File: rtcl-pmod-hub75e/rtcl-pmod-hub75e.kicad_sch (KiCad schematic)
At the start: 22 parts, among them J1 PMOD, J2 HIF3FC-16PA-2.54DSA(71), J3 Conn_01x02, U1 74LVC273, U2 74LVC273, U3 74LVC273, U4 74LVC273, U5 LM809M3-2.93, U6 74LVC2G86

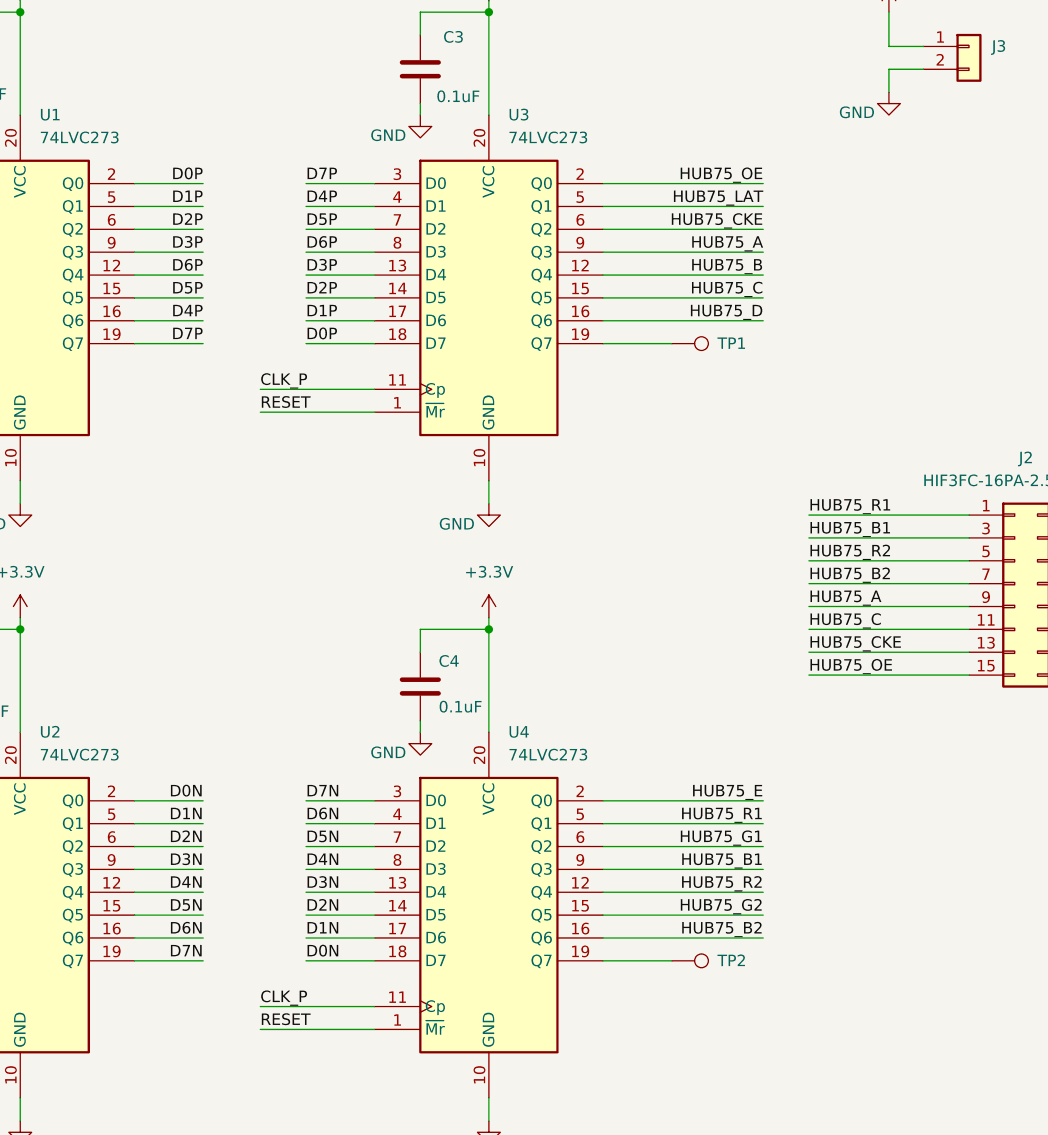
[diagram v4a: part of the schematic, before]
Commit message: Update active layer and adjust wire positions in schematic
- Changed active layer from 0 to 2 in the PCB layout.
- Adjusted multiple wire coordinates in the schematic to correct alignment.
- Updated label positions for various components to ensure proper placement.
- Modified test point coordinates for better alignment with the design.
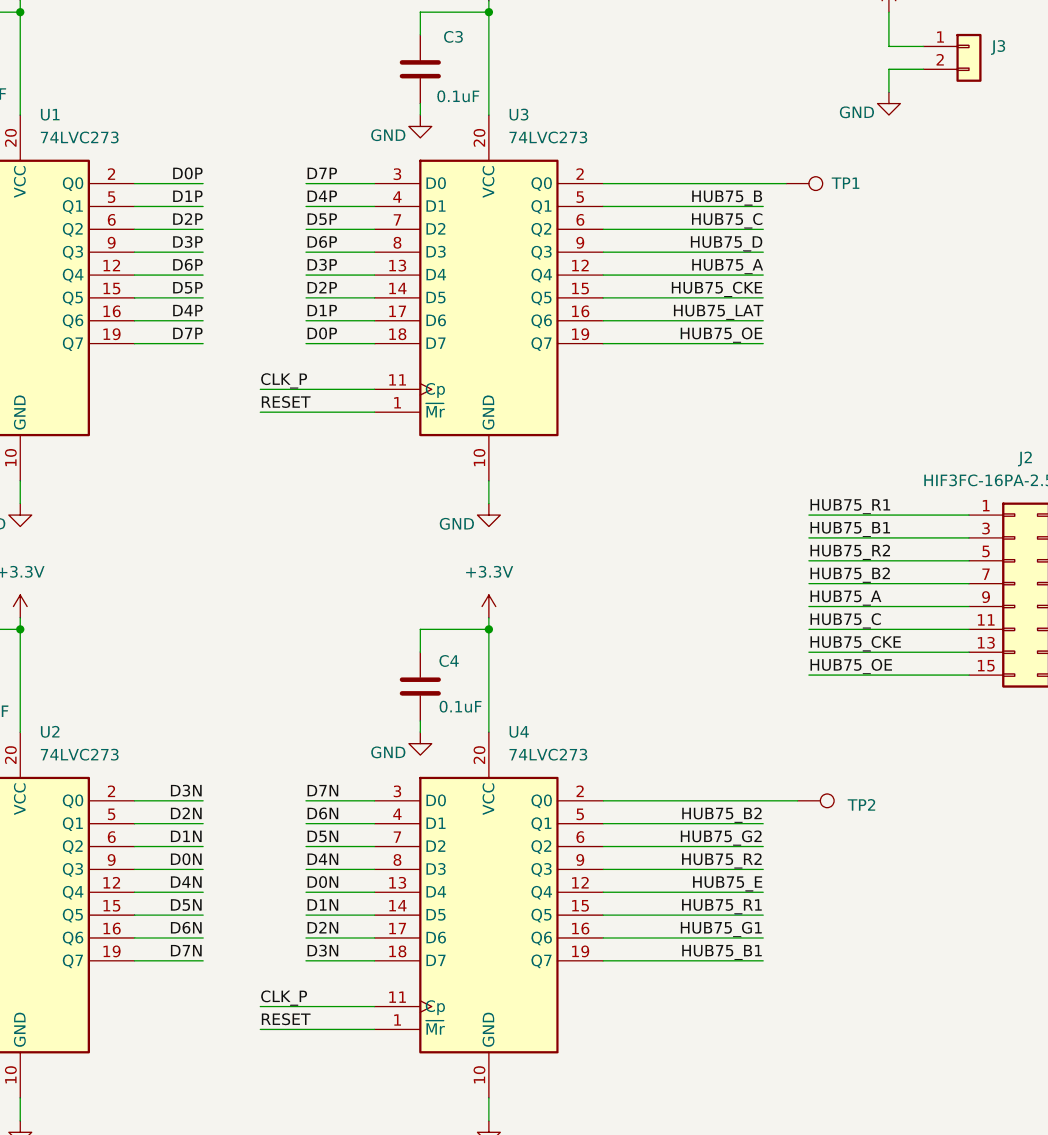
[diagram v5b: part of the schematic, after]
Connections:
- net D0N: now also U2.9 (Q3), U4.13 (D4); no longer U2.2 (Q0), U4.18 (D7)
- net D1N: now also U2.6 (Q2), U4.14 (D5); no longer U2.5 (Q1), U4.17 (D6)
- net D2N: now also U2.5 (Q1), U4.17 (D6); no longer U2.6 (Q2), U4.14 (D5)
- net D3N: now also U2.2 (Q0), U4.18 (D7); no longer U2.9 (Q3), U4.13 (D4)
- net HUB75_A: now also U3.12 (Q4); no longer U3.9 (Q3)
- net HUB75_B: now also U3.5 (Q1); no longer U3.12 (Q4)
- net HUB75_B1: now also U4.19 (Q7); no longer U4.9 (Q3)
- net HUB75_B2: now also U4.5 (Q1); no longer U4.16 (Q6)
- net HUB75_C: now also U3.6 (Q2); no longer U3.15 (Q5)
- net HUB75_CKE: now also U3.15 (Q5); no longer U3.6 (Q2)
- net HUB75_D: now also U3.9 (Q3); no longer U3.16 (Q6)
- net HUB75_E: now also U4.12 (Q4); no longer U4.2 (Q0)
- net HUB75_G1: now also U4.16 (Q6); no longer U4.6 (Q2)
- net HUB75_G2: now also U4.6 (Q2); no longer U4.15 (Q5)
- net HUB75_LAT: now also U3.16 (Q6); no longer U3.5 (Q1)
- net HUB75_OE: now also U3.19 (Q7); no longer U3.2 (Q0)
- net HUB75_R1: now also U4.15 (Q5); no longer U4.5 (Q1)
- net HUB75_R2: now also U4.9 (Q3); no longer U4.12 (Q4)
- net at TP2.1: now also U4.2 (Q0); no longer U4.19 (Q7)
- net at TP1.1: now also U3.2 (Q0); no longer U3.19 (Q7)
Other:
- moved on the sheet: TP1, TP2
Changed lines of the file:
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@@
 	(wire
 		(pts
-			(xy 168.91 127) (xy 176.53 127)
+			(xy 168.91 134.62) (xy 176.53 134.62)
 		)
 		(stroke
@@
 	(wire
 		(pts
-			(xy 219.71 121.92) (xy 201.93 121.92)
+			(xy 219.71 132.08) (xy 201.93 132.08)
 		)
 		(stroke
@@
 	(wire
 		(pts
-			(xy 157.48 119.38) (xy 149.86 119.38)
+			(xy 157.48 121.92) (xy 149.86 121.92)
 		)
 		(stroke
@@
 	(wire
 		(pts
-			(xy 219.71 119.38) (xy 201.93 119.38)
+			(xy 219.71 129.54) (xy 201.93 129.54)
 		)
 		(stroke
@@
 	(wire
 		(pts
-			(xy 168.91 132.08) (xy 176.53 132.08)
+			(xy 168.91 129.54) (xy 176.53 129.54)
 		)
 		(stroke
@@
 	(wire
 		(pts
-			(xy 219.71 124.46) (xy 201.93 124.46)
+			(xy 219.71 134.62) (xy 201.93 134.62)
 		)
 		(stroke
@@
 	(wire
 		(pts
-			(xy 219.71 129.54) (xy 201.93 129.54)
+			(xy 219.71 121.92) (xy 201.93 121.92)
 		)
 		(stroke
@@
 	(wire
 		(pts
-			(xy 219.71 48.26) (xy 201.93 48.26)
+			(xy 219.71 66.04) (xy 201.93 66.04)
 		)
 		(stroke
@@
 	(wire
 		(pts
-			(xy 219.71 132.08) (xy 201.93 132.08)
+			(xy 219.71 119.38) (xy 201.93 119.38)
 		)
 		(stroke
@@
 	(wire
 		(pts
-			(xy 219.71 63.5) (xy 201.93 63.5)
+			(xy 219.71 55.88) (xy 201.93 55.88)
 		)
 		(stroke
@@
 	(wire
 		(pts
-			(xy 219.71 116.84) (xy 201.93 116.84)
+			(xy 219.71 127) (xy 201.93 127)
 		)
 		(stroke
@@
 	(wire
 		(pts
-			(xy 201.93 66.04) (xy 209.55 66.04)
+			(xy 201.93 48.26) (xy 222.25 48.26)
 		)
 		(stroke
@@
 	(wire
 		(pts
-			(xy 201.93 134.62) (xy 209.55 134.62)
+			(xy 201.93 116.84) (xy 223.52 116.84)
 		)
 		(stroke
@@
 	(wire
 		(pts
-			(xy 157.48 124.46) (xy 149.86 124.46)
+			(xy 157.48 116.84) (xy 149.86 116.84)
 		)
 		(stroke
@@
 	(wire
 		(pts
-			(xy 157.48 116.84) (xy 149.86 116.84)
+			(xy 157.48 124.46) (xy 149.86 124.46)
 		)
 		(stroke
@@
 	(wire
 		(pts
-			(xy 219.71 50.8) (xy 201.93 50.8)
+			(xy 219.71 63.5) (xy 201.93 63.5)
 		)
 		(stroke
@@
 	(wire
 		(pts
-			(xy 168.91 134.62) (xy 176.53 134.62)
+			(xy 168.91 127) (xy 176.53 127)
 		)
 		(stroke
@@
 	(wire
 		(pts
-			(xy 219.71 53.34) (xy 201.93 53.34)
+			(xy 219.71 60.96) (xy 201.93 60.96)
 		)
 		(stroke
@@
 	(wire
 		(pts
-			(xy 157.48 121.92) (xy 149.86 121.92)
+			(xy 157.48 119.38) (xy 149.86 119.38)
 		)
 		(stroke
@@
 	(wire
 		(pts
-			(xy 219.71 58.42) (xy 201.93 58.42)
+			(xy 219.71 50.8) (xy 201.93 50.8)
 		)
 		(stroke
@@
 	(wire
 		(pts
-			(xy 168.91 129.54) (xy 176.53 129.54)
+			(xy 168.91 132.08) (xy 176.53 132.08)
 		)
 		(stroke
@@
 	(wire
 		(pts
-			(xy 219.71 127) (xy 201.93 127)
+			(xy 219.71 124.46) (xy 201.93 124.46)
 		)
 		(stroke
@@
 	(wire
 		(pts
-			(xy 219.71 60.96) (xy 201.93 60.96)
+			(xy 219.71 53.34) (xy 201.93 53.34)
 		)
 		(stroke
@@
 	(wire
 		(pts
-			(xy 219.71 55.88) (xy 201.93 55.88)
+			(xy 219.71 58.42) (xy 201.93 58.42)
 		)
 		(stroke
@@
 	)
 	(label "D3N"
-		(at 157.48 124.46 180)
+		(at 157.48 116.84 180)
 		(effects
 			(font
@@
 	)
 	(label "D1N"
-		(at 168.91 132.08 0)
+		(at 168.91 129.54 0)
 		(effects
 			(font
@@
 	)
 	(label "HUB75_B"
-		(at 219.71 58.42 180)
+		(at 219.71 50.8 180)
 		(effects
 			(font
@@
 	)
 	(label "D0N"
-		(at 157.48 116.84 180)
+		(at 157.48 124.46 180)
 		(effects
 			(font
@@
 	)
 	(label "D1N"
-		(at 157.48 119.38 180)
+		(at 157.48 121.92 180)
 		(effects
 			(font
@@
 	)
 	(label "HUB75_G2"
-		(at 219.71 129.54 180)
+		(at 219.71 121.92 180)
 		(effects
 			(font
@@
 	)
 	(label "HUB75_LAT"
-		(at 219.71 50.8 180)
+		(at 219.71 63.5 180)
 		(effects
 			(font
@@
 	)
 	(label "HUB75_G1"
-		(at 219.71 121.92 180)
+		(at 219.71 132.08 180)
 		(effects
 			(font
@@
 	)
 	(label "D3N"
-		(at 168.91 127 0)
+		(at 168.91 134.62 0)
 		(effects
 			(font
@@
 	)
 	(label "HUB75_D"
-		(at 219.71 63.5 180)
+		(at 219.71 55.88 180)
 		(effects
 			(font
@@
 	)
 	(label "HUB75_C"
-		(at 219.71 60.96 180)
+		(at 219.71 53.34 180)
 		(effects
 			(font
@@
 	)
 	(label "HUB75_OE"
-		(at 219.71 48.26 180)
+		(at 219.71 66.04 180)
 		(effects
 			(font
@@
 	)
 	(label "HUB75_CKE"
-		(at 219.71 53.34 180)
+		(at 219.71 60.96 180)
 		(effects
 			(font
@@
 	)
 	(label "HUB75_R1"
-		(at 219.71 119.38 180)
+		(at 219.71 129.54 180)
 		(effects
 			(font
@@
 	)
 	(label "HUB75_R2"
-		(at 219.71 127 180)
+		(at 219.71 124.46 180)
 		(effects
 			(font
@@
 	)
 	(label "HUB75_A"
-		(at 219.71 55.88 180)
+		(at 219.71 58.42 180)
 		(effects
 			(font
@@
 	)
 	(label "HUB75_E"
-		(at 219.71 116.84 180)
+		(at 219.71 127 180)
 		(effects
 			(font
@@
 	)
 	(label "D2N"
-		(at 157.48 121.92 180)
+		(at 157.48 119.38 180)
 		(effects
 			(font
@@
 	)
 	(label "D2N"
-		(at 168.91 129.54 0)
+		(at 168.91 132.08 0)
 		(effects
 			(font
@@
 	)
 	(label "HUB75_B1"
-		(at 219.71 124.46 180)
+		(at 219.71 134.62 180)
 		(effects
 			(font
@@
 	)
 	(label "HUB75_B2"
-		(at 219.71 132.08 180)
+		(at 219.71 119.38 180)
 		(effects
 			(font
@@
 	)
 	(label "D0N"
-		(at 168.91 134.62 0)
+		(at 168.91 127 0)
 		(effects
 			(font
@@
 	(symbol
 		(lib_id "Connector:TestPoint")
-		(at 209.55 134.62 270)
+		(at 223.52 116.84 270)
 		(unit 1)
 		(body_style 1)
@@
 		(dnp no)
 		(property "Reference" "TP2"
-			(at 214.63 134.62 90)
+			(at 229.108 117.348 90)
 			(show_name no)
 			(do_not_autoplace no)
@@
 		)
 		(property "Value" "TestPoint"
-			(at 214.63 135.8899 90)
+			(at 228.6 118.1099 90)
 			(hide yes)
 			(show_name no)
@@
 		)
 		(property "Footprint" "TestPoint:TestPoint_Pad_D1.0mm"
-			(at 209.55 139.7 0)
+			(at 223.52 121.92 0)
 			(hide yes)
 			(show_name no)
@@
 		)
 		(property "Datasheet" ""
-			(at 209.55 139.7 0)
+			(at 223.52 121.92 0)
 			(hide yes)
 			(show_name no)
@@
 		)
 		(property "Description" "test point"
-			(at 209.55 134.62 0)
+			(at 223.52 116.84 0)
 			(hide yes)
 			(show_name no)
@@
 	(symbol
 		(lib_id "Connector:TestPoint")
-		(at 209.55 66.04 270)
+		(at 222.25 48.26 270)
 		(unit 1)
 		(body_style 1)
@@
 		(dnp no)
 		(property "Reference" "TP1"
-			(at 214.63 66.04 90)
+			(at 227.33 48.26 90)
 			(show_name no)
 			(do_not_autoplace no)
@@
 		)
 		(property "Value" "TestPoint"
-			(at 214.63 67.3099 90)
+			(at 227.33 49.5299 90)
 			(hide yes)
 			(show_name no)
@@
 		)
 		(property "Footprint" "TestPoint:TestPoint_Pad_D1.0mm"
-			(at 209.55 71.12 0)
+			(at 222.25 53.34 0)
 			(hide yes)
 			(show_name no)
@@
 		)
 		(property "Datasheet" ""
-			(at 209.55 71.12 0)
+			(at 222.25 53.34 0)
 			(hide yes)
 			(show_name no)
@@
 		)
 		(property "Description" "test point"
-			(at 209.55 66.04 0)
+			(at 222.25 48.26 0)
 			(hide yes)
 			(show_name no)

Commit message: Update PCB and schematic files for rtcl-pmod-hub75e
- Changed active layer from 2 to 5 in the PCB layout.
- Modified visibility settings for text, tracks, and vias in the PCB layout.
- Updated visible layers in the PCB layout.
- Changed footprint references from "TestPoint" to "rtcl-pmod-hub75e" in the schematic.
- Updated UUIDs for various elements in the PH_02x08_2.54mm footprint.
- Added new footprint for TestPoint_Pad_D1.0mm.
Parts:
- TP1, TP2, TP3, TP4: footprint TestPoint:TestPoint_Pad_D1.0mm -> rtcl-pmod-hub75e:TestPoint_Pad_D1.0mm
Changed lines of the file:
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@@
 			)
 		)
-		(property "Footprint" "TestPoint:TestPoint_Pad_D1.0mm"
+		(property "Footprint" "rtcl-pmod-hub75e:TestPoint_Pad_D1.0mm"
 			(at 97.79 129.54 0)
 			(hide yes)
@@
 			)
 		)
-		(property "Footprint" "TestPoint:TestPoint_Pad_D1.0mm"
+		(property "Footprint" "rtcl-pmod-hub75e:TestPoint_Pad_D1.0mm"
 			(at 223.52 121.92 0)
 			(hide yes)
@@
 			)
 		)
-		(property "Footprint" "TestPoint:TestPoint_Pad_D1.0mm"
+		(property "Footprint" "rtcl-pmod-hub75e:TestPoint_Pad_D1.0mm"
 			(at 222.25 53.34 0)
 			(hide yes)
@@
 			)
 		)
-		(property "Footprint" "TestPoint:TestPoint_Pad_D1.0mm"
+		(property "Footprint" "rtcl-pmod-hub75e:TestPoint_Pad_D1.0mm"
 			(at 97.79 60.96 0)
 			(hide yes)

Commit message: Add LCSC properties for components in schematic
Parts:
- J1: LCSC (none) -> C124371
- J2: LCSC (none) -> C7430313
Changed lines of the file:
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@@
+			)
+		)
+		(property "LCSC" "C7430313"
+			(at 247.65 92.71 0)
+			(hide yes)
+			(show_name no)
+			(do_not_autoplace no)
+			(effects
+				(font
+					(size 1.27 1.27)
+				)
 			)
 		)
@@
 			(at 52.07 43.18 0)
 			(hide yes)
+			(show_name no)
+			(do_not_autoplace no)
+			(effects
+				(font
+					(size 1.27 1.27)
+				)
+			)
+		)
+		(property "LCSC" "C124371"
+			(at 52.07 43.18 0)
+			(hide yes)

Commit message: wip
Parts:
- J2: value HIF3FC-16PA-2.54DSA(71) -> HUB75E
- U6: value 74LVC2G86 -> SN74LVC2G86DCUR
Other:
- note added: "min:1.6ns/max:4.7ns"
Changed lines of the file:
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@@
 	(generator_version "10.0")
 	(paper "A4")
+	(text "min:1.6ns/max:4.7ns"
+		(exclude_from_sim no)
+		(at 80.518 193.802 0)
+		(effects
+			(font
+				(size 1.27 1.27)
+			)
+		)
+	)
+	(text ""
+		(exclude_from_sim no)
+		(at 138.684 135.89 0)
+		(effects
+			(font
+				(size 1.27 1.27)
+			)
+		)
+	)
 	(junction
 		(at 189.23 29.21)
@@
 			)
 		)
-		(property "Value" "74LVC2G86"
-			(at 85.09 177.8 0)
+		(property "Value" "SN74LVC2G86DCUR"
+			(at 88.392 177.8 0)
 			(show_name no)
 			(do_not_autoplace no)
@@
 			)
 		)
-		(property "Value" "74LVC2G86"
+		(property "Value" "SN74LVC2G86DCUR"
 			(at 57.15 137.1599 0)
 			(show_name no)
@@
 			)
 		)
-		(property "Value" "74LVC2G86"
-			(at 83.566 161.29 0)
+		(property "Value" "SN74LVC2G86DCUR"
+			(at 87.884 161.036 0)
 			(show_name no)
 			(do_not_autoplace no)
@@
 			)
 		)
-		(property "Value" "HIF3FC-16PA-2.54DSA(71)"
+		(property "Value" "HUB75E"
 			(at 248.92 81.28 0)
 			(show_name no)
